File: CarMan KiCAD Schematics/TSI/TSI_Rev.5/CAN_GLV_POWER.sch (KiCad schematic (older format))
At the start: 35 parts, among them Q11 TN2130K1-G, U14 MountingHole, U15 MountingHole, U17 ChassisGND, U2 SFS2-DC24V, U24 TLP293, U28 MountingHole, U33 SFS2-DC24V, U41 PDQ10-Q24-D5-D, U42 LT1763CS8-3.3PBF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

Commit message: TSI Footprints - Res, Caps, Inductor all 0805s - Mounting Holes
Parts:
- removed U17: ChassisGND, symbol Mechanical:MountingHole
- added U17: Chassis Ground, MountingHole:MountingHole_3.5mm_Pad, symbol Mechanical:MountingHole_Pad
- C13, C18, C56, C57, C58, C59, C60, C61: footprint (none) -> Capacitor_SMD:C_0805_2012Metric_Pad1.15x1.40mm_HandSolder
- R45, R52, R55, R57, R71, R72, R79, R92: footprint (none) -> Resistor_SMD:R_0805_2012Metric_Pad1.15x1.40mm_HandSolder
- U14, U15, U28: footprint (none) -> MountingHole:MountingHole_3.5mm_Pad
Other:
- moved on the sheet: U14, U15, U28
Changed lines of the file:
@@
 L Mechanical:MountingHole U14
 U 1 1 5FB208C3
-P 900 800
-F 0 "U14" H 800 950 50  0000 L CNN
-F 1 "MountingHole" H 650 650 50  0000 L CNN
-F 2 "" H 900 800 50  0001 C CNN
-F 3 "~" H 900 800 50  0001 C CNN
-	1    900  800
+P 800 800
+F 0 "U14" H 700 950 50  0000 L CNN
+F 1 "MountingHole" H 550 650 50  0000 L CNN
+F 2 "MountingHole:MountingHole_3.5mm_Pad" H 800 800 50  0001 C CNN
+F 3 "~" H 800 800 50  0001 C CNN
+	1    800  800
 	1    0    0    -1
 $EndComp
@@
 L Mechanical:MountingHole U15
 U 1 1 5FB22D5E
-P 1550 800
-F 0 "U15" H 1450 950 50  0000 L CNN
-F 1 "MountingHole" H 1300 650 50  0000 L CNN
-F 2 "" H 1550 800 50  0001 C CNN
-F 3 "~" H 1550 800 50  0001 C CNN
-	1    1550 800
+P 1450 800
+F 0 "U15" H 1350 950 50  0000 L CNN
+F 1 "MountingHole" H 1200 650 50  0000 L CNN
+F 2 "MountingHole:MountingHole_3.5mm_Pad" H 1450 800 50  0001 C CNN
+F 3 "~" H 1450 800 50  0001 C CNN
+	1    1450 800
 	1    0    0    -1
 $EndComp
@@
 L Mechanical:MountingHole U28
 U 1 1 5FB236B2
-P 2200 800
-F 0 "U28" H 2100 950 50  0000 L CNN
-F 1 "MountingHole" H 1950 650 50  0000 L CNN
-F 2 "" H 2200 800 50  0001 C CNN
-F 3 "~" H 2200 800 50  0001 C CNN
-	1    2200 800
-	1    0    0    -1
-$EndComp
-$Comp
-L Mechanical:MountingHole U17
-U 1 1 5FB23CBE
-P 900 1250
-F 0 "U17" H 700 1350 50  0000 L CNN
-F 1 "ChassisGND" H 650 1100 50  0000 L CNN
-F 2 "" H 900 1250 50  0001 C CNN
-F 3 "~" H 900 1250 50  0001 C CNN
-	1    900  1250
+P 800 1300
+F 0 "U28" H 700 1450 50  0000 L CNN
+F 1 "MountingHole" H 550 1150 50  0000 L CNN
+F 2 "MountingHole:MountingHole_3.5mm_Pad" H 800 1300 50  0001 C CNN
+F 3 "~" H 800 1300 50  0001 C CNN
+	1    800  1300
 	1    0    0    -1
 $EndComp
@@
 F 0 "C57" H 1900 4900 50  0000 L CNN
 F 1 "10u" H 1850 4700 50  0000 L CNN
-F 2 "" H 1850 4800 50  0001 C CNN
+F 2 "Capacitor_SMD:C_0805_2012Metric_Pad1.15x1.40mm_HandSolder" H 1850 4800 50  0001 C CNN
 F 3 "~" H 1850 4800 50  0001 C CNN
 	1    1850 4800
@@
 F 0 "C56" H 1350 4900 50  0000 L CNN
 F 1 "10u" H 1350 4700 50  0000 L CNN
-F 2 "" H 1350 4800 50  0001 C CNN
+F 2 "Capacitor_SMD:C_0805_2012Metric_Pad1.15x1.40mm_HandSolder" H 1350 4800 50  0001 C CNN
 F 3 "~" H 1350 4800 50  0001 C CNN
 	1    1350 4800
@@
 F 0 "C58" H 4700 5300 50  0000 L CNN
 F 1 "0.1u" H 4700 5100 50  0000 L CNN
-F 2 "" H 4700 5200 50  0001 C CNN
+F 2 "Capacitor_SMD:C_0805_2012Metric_Pad1.15x1.40mm_HandSolder" H 4700 5200 50  0001 C CNN
 F 3 "~" H 4700 5200 50  0001 C CNN
 	1    4700 5200
@@
 F 0 "C59" H 5400 5550 50  0000 L CNN
 F 1 "1u" H 5400 5350 50  0000 L CNN
-F 2 "" H 5350 5450 50  0001 C CNN
+F 2 "Capacitor_SMD:C_0805_2012Metric_Pad1.15x1.40mm_HandSolder" H 5350 5450 50  0001 C CNN
 F 3 "~" H 5350 5450 50  0001 C CNN
 	1    5350 5450
@@
 F 0 "C60" H 5900 5350 50  0000 L CNN
 F 1 "1u" H 5900 5150 50  0000 L CNN
-F 2 "" H 6100 5250 50  0001 C CNN
+F 2 "Capacitor_SMD:C_0805_2012Metric_Pad1.15x1.40mm_HandSolder" H 6100 5250 50  0001 C CNN
 F 3 "~" H 6100 5250 50  0001 C CNN
 	1    6100 5250
@@
 Text Label 15050 1050 2    50   ~ 0
 CANRX
-Wire Wire Line
-	900  1250 1400 1250
-Text Label 1400 1250 0    50   ~ 0
+Text Label 2050 1300 2    50   ~ 0
 ChassisGND
 Text Notes 7750 4000 2    89   ~ 0
@@
 F 0 "C61" H 8150 5500 50  0000 L CNN
 F 1 "10u" H 8150 5300 50  0000 L CNN
-F 2 "" H 8100 5400 50  0001 C CNN
+F 2 "Capacitor_SMD:C_0805_2012Metric_Pad1.15x1.40mm_HandSolder" H 8100 5400 50  0001 C CNN
 F 3 "~" H 8100 5400 50  0001 C CNN
 	1    8100 5400
@@
 F 0 "R92" V 11000 3600 50  0000 C CNN
 F 1 "120" V 11100 3600 50  0000 C CNN
-F 2 "" V 11030 3600 50  0001 C CNN
+F 2 "Resistor_SMD:R_0805_2012Metric_Pad1.15x1.40mm_HandSolder" V 11030 3600 50  0001 C CNN
 F 3 "~" H 11100 3600 50  0001 C CNN
 	1    11100 3600
@@
 F 0 "R71" V 3900 1050 50  0000 C CNN
 F 1 "2.1K" V 4000 1050 50  0000 C CNN
-F 2 "" V 3930 1050 50  0001 C CNN
+F 2 "Resistor_SMD:R_0805_2012Metric_Pad1.15x1.40mm_HandSolder" V 3930 1050 50  0001 C CNN
 F 3 "~" H 4000 1050 50  0001 C CNN
 	1    4000 1050
@@
 F 0 "R79" H 10970 6196 50  0000 L CNN
 F 1 "10K" V 10900 6100 50  0000 L CNN
-F 2 "" V 10830 6150 50  0001 C CNN
+F 2 "Resistor_SMD:R_0805_2012Metric_Pad1.15x1.40mm_HandSolder" V 10830 6150 50  0001 C CNN
 F 3 "~" H 10900 6150 50  0001 C CNN
 	1    10900 6150
@@
 F 0 "R72" V 10650 5900 50  0000 C CNN
 F 1 "1K" V 10750 5900 50  0000 C CNN
-F 2 "" V 10680 5900 50  0001 C CNN
+F 2 "Resistor_SMD:R_0805_2012Metric_Pad1.15x1.40mm_HandSolder" V 10680 5900 50  0001 C CNN
 F 3 "~" H 10750 5900 50  0001 C CNN
 	1    10750 5900
@@
 F 0 "R45" V 9300 1300 50  0000 C CNN
 F 1 "2.4K" V 9400 1300 50  0000 C CNN
-F 2 "" V 9330 1300 50  0001 C CNN
+F 2 "Resistor_SMD:R_0805_2012Metric_Pad1.15x1.40mm_HandSolder" V 9330 1300 50  0001 C CNN
 F 3 "~" H 9400 1300 50  0001 C CNN
 	1    9400 1300
@@
 F 0 "R55" V 10450 1100 50  0000 C CNN
 F 1 "2.4K" V 10550 1100 50  0000 C CNN
-F 2 "" V 10480 1100 50  0001 C CNN
+F 2 "Resistor_SMD:R_0805_2012Metric_Pad1.15x1.40mm_HandSolder" V 10480 1100 50  0001 C CNN
 F 3 "~" H 10550 1100 50  0001 C CNN
 	1    10550 1100
@@
 F 0 "R52" H 12320 3346 50  0000 L CNN
 F 1 "1K" H 12350 3250 50  0000 L CNN
-F 2 "" V 12180 3300 50  0001 C CNN
+F 2 "Resistor_SMD:R_0805_2012Metric_Pad1.15x1.40mm_HandSolder" V 12180 3300 50  0001 C CNN
 F 3 "~" H 12250 3300 50  0001 C CNN
 	1    12250 3300
@@
 F 0 "R57" H 5270 1496 50  0000 L CNN
 F 1 "40K" H 5270 1405 50  0000 L CNN
-F 2 "" V 5130 1450 50  0001 C CNN
+F 2 "Resistor_SMD:R_0805_2012Metric_Pad1.15x1.40mm_HandSolder" V 5130 1450 50  0001 C CNN
 F 3 "~" H 5200 1450 50  0001 C CNN
 	1    5200 1450
@@
 F 0 "C18" H 6765 2446 50  0000 L CNN
 F 1 "10u" H 6765 2355 50  0000 L CNN
-F 2 "" H 6688 2250 50  0001 C CNN
+F 2 "Capacitor_SMD:C_0805_2012Metric_Pad1.15x1.40mm_HandSolder" H 6688 2250 50  0001 C CNN
 F 3 "~" H 6650 2400 50  0001 C CNN
 	1    6650 2400
@@
 F 0 "C13" H 4165 2446 50  0000 L CNN
 F 1 "100u" H 4165 2355 50  0000 L CNN
-F 2 "" H 4088 2250 50  0001 C CNN
+F 2 "Capacitor_SMD:C_0805_2012Metric_Pad1.15x1.40mm_HandSolder" H 4088 2250 50  0001 C CNN
 F 3 "~" H 4050 2400 50  0001 C CNN
 	1    4050 2400
@@
 Text Notes 3650 3000 0    55   ~ 0
 Control Signal used as a \npsuedo relay
+$Comp
+L Mechanical:MountingHole_Pad U17
+U 1 1 60035C0C
+P 1500 1300
+F 0 "U17" V 1650 1350 50  0000 C CNN
+F 1 "Chassis Ground" V 1350 1300 50  0000 C CNN
+F 2 "MountingHole:MountingHole_3.5mm_Pad" H 1500 1300 50  0001 C CNN
+F 3 "~" H 1500 1300 50  0001 C CNN
+	1    1500 1300
+	0    -1   -1   0
+$EndComp
+Wire Wire Line
+	1600 1300 2050 1300
 $EndSCHEMATC

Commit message: TSI Footprinting (~80%)  - Added Molex  - Added Current Sensor
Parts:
- 3.3V_TP1, 5V_TP1: footprint (none) -> TestPoint:TestPoint_Pad_D3.0mm
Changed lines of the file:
@@
 F 0 "5V_TP1" H 5008 4918 50  0000 L CNN
 F 1 "5V_TP" H 5008 4827 50  0000 L CNN
-F 2 "" H 5150 4800 50  0001 C CNN
+F 2 "TestPoint:TestPoint_Pad_D3.0mm" H 5150 4800 50  0001 C CNN
 F 3 "~" H 5150 4800 50  0001 C CNN
 	1    4950 4800
@@
 F 0 "3.3V_TP1" H 8150 4900 50  0001 L TNN
 F 1 "3.3V_TP" H 8150 4850 50  0000 L CNN
-F 2 "" H 8500 4650 50  0001 C CNN
+F 2 "TestPoint:TestPoint_Pad_D3.0mm" H 8500 4650 50  0001 C CNN
 F 3 "~" H 8500 4650 50  0001 C CNN
 	1    8300 4650

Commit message: TSI Footprinting (~90%)
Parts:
- D5, D9: footprint Diode_THT:D_DO-41_SOD81_P10.16mm_Horizontal -> Diode_THT:D_DO-41_SOD81_P7.62mm_Horizontal
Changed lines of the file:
@@
 F 0 "D9" H 3150 7500 50  0000 L CNN
 F 1 "1N4001" H 3050 7700 50  0000 L CNN
-F 2 "Diode_THT:D_DO-41_SOD81_P10.16mm_Horizontal" H 3200 7425 50  0001 C CNN
+F 2 "Diode_THT:D_DO-41_SOD81_P7.62mm_Horizontal" H 3200 7425 50  0001 C CNN
 F 3 "http://www.vishay.com/docs/88503/1n4001.pdf" H 3200 7600 50  0001 C CNN
 	1    3200 7600
@@
 F 0 "D5" H 8150 7450 50  0000 L CNN
 F 1 "1N4001" H 8050 7650 50  0000 L CNN
-F 2 "Diode_THT:D_DO-41_SOD81_P10.16mm_Horizontal" H 8200 7375 50  0001 C CNN
+F 2 "Diode_THT:D_DO-41_SOD81_P7.62mm_Horizontal" H 8200 7375 50  0001 C CNN
 F 3 "http://www.vishay.com/docs/88503/1n4001.pdf" H 8200 7550 50  0001 C CNN
 	1    8200 7550

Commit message: Bug Fixins
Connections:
- net labels removed: ChassisGND
- wire segments 179 -> 177
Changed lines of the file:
@@
 Wire Wire Line
 	4700 4950 4700 4800
-Wire Wire Line
-	3650 4800 4550 4800
-$Comp
-L power:PWR_FLAG #FLG03
-U 1 1 5FB2DC71
-P 4550 4800
-F 0 "#FLG03" H 4550 4875 50  0001 C CNN
-F 1 "PWR_FLAG" H 4450 4750 50  0000 C CNN
-F 2 "" H 4550 4800 50  0001 C CNN
-F 3 "~" H 4550 4800 50  0001 C CNN
-	1    4550 4800
-	1    0    0    -1
-$EndComp
-Connection ~ 4550 4800
-Wire Wire Line
-	4550 4800 4700 4800
 $Comp
 L pspice:CAP C59
@@
 CANRX
 Text Label 2050 1300 2    50   ~ 0
-ChassisGND
+Chassis_GND
 Text Notes 7750 4000 2    89   ~ 0
 3.3V REGULATOR
@@
 Wire Wire Line
 	3650 4700 4350 4700
-$Comp
-L power:PWR_FLAG #FLG0103
-U 1 1 60AD6C72
-P 4350 4700
-F 0 "#FLG0103" H 4350 4775 50  0001 C CNN
-F 1 "PWR_FLAG" H 4350 4873 50  0000 C CNN
-F 2 "" H 4350 4700 50  0001 C CNN
-F 3 "~" H 4350 4700 50  0001 C CNN
-	1    4350 4700
-	1    0    0    -1
-$EndComp
 Text Notes 10950 1900 2    89   ~ 0
 AIRs power on SL closed
@@
 Text Notes 3700 2050 0    49   ~ 0
 DC/DC Converter 24V to 12V 10A
-Wire Wire Line
-	6450 2250 6650 2250
-Connection ~ 6450 2250
-$Comp
-L power:PWR_FLAG #FLG02
-U 1 1 5FBAC9F1
-P 6450 2250
-F 0 "#FLG02" H 6450 2325 50  0001 C CNN
-F 1 "PWR_FLAG" H 6450 2423 50  0000 C CNN
-F 2 "" H 6450 2250 50  0001 C CNN
-F 3 "~" H 6450 2250 50  0001 C CNN
-	1    6450 2250
-	1    0    0    -1
-$EndComp
 Text Label 3250 2650 0    49   ~ 0
 GLV_RTN
@@
 Wire Wire Line
 	6650 2550 6650 2650
-Wire Wire Line
-	6250 2250 6450 2250
 Wire Wire Line
 	4950 2650 5050 2650
@@
 Wire Wire Line
 	1600 1300 2050 1300
+Wire Wire Line
+	6250 2250 6650 2250
+Wire Wire Line
+	3650 4800 4700 4800
 $EndSCHEMATC

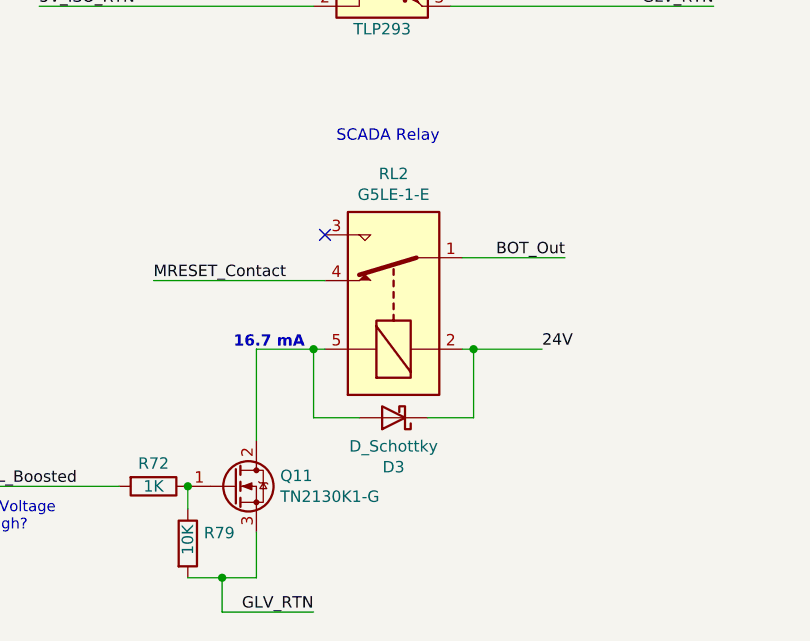
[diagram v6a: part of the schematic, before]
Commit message: TSI Footprinting (~95%) - Added Silk Screen Images from last years projects (not added to any libraries, just folder)
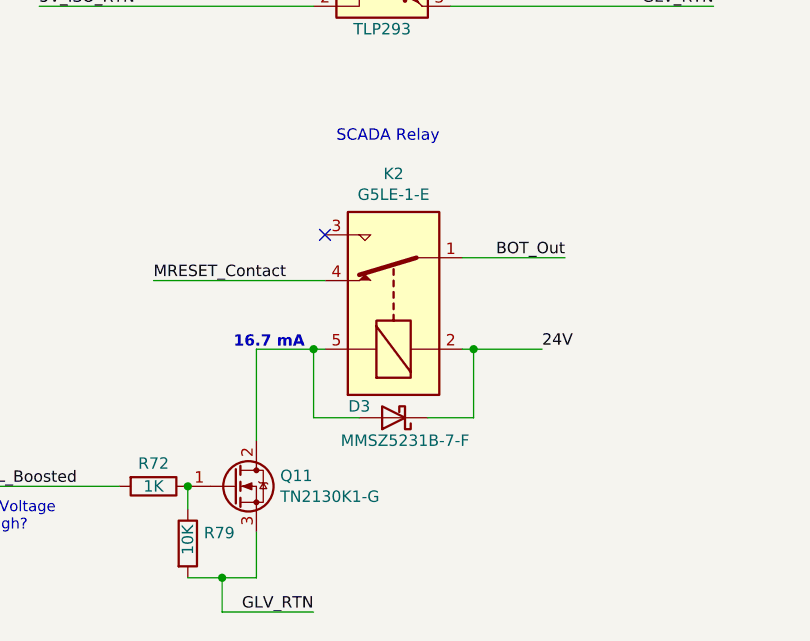
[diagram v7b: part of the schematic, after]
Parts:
- D3: value D_Schottky -> MMSZ5231B-7-F; footprint (none) -> Diode_SMD:D_SOD-123
- renumbered RL2 to K2
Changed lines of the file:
@@
 U 1 1 5FB8F043
 P 11800 5600
-F 0 "D3" H 11800 5816 50  0000 C CNN
-F 1 "D_Schottky" H 11800 5725 50  0000 C CNN
-F 2 "" H 11800 5600 50  0001 C CNN
+F 0 "D3" H 11950 5550 50  0000 C CNN
+F 1 "MMSZ5231B-7-F" H 11750 5700 50  0000 C CNN
+F 2 "Diode_SMD:D_SOD-123" H 11800 5600 50  0001 C CNN
 F 3 "~" H 11800 5600 50  0001 C CNN
 	1    11800 5600
@@
 P 11800 5100
 AR Path="/5FB466B1" Ref="RL?"  Part="1"
-AR Path="/5FE1DE7D/5FB466B1" Ref="RL2"  Part="1"
-F 0 "RL2" V 12367 5100 50  0000 C CNN
+AR Path="/5FE1DE7D/5FB466B1" Ref="K2"  Part="1"
+F 0 "K2" V 12367 5100 50  0000 C CNN
 F 1 "G5LE-1-E" V 12276 5100 50  0000 C CNN
 F 2 "" H 12050 5700 50  0001 C CNN

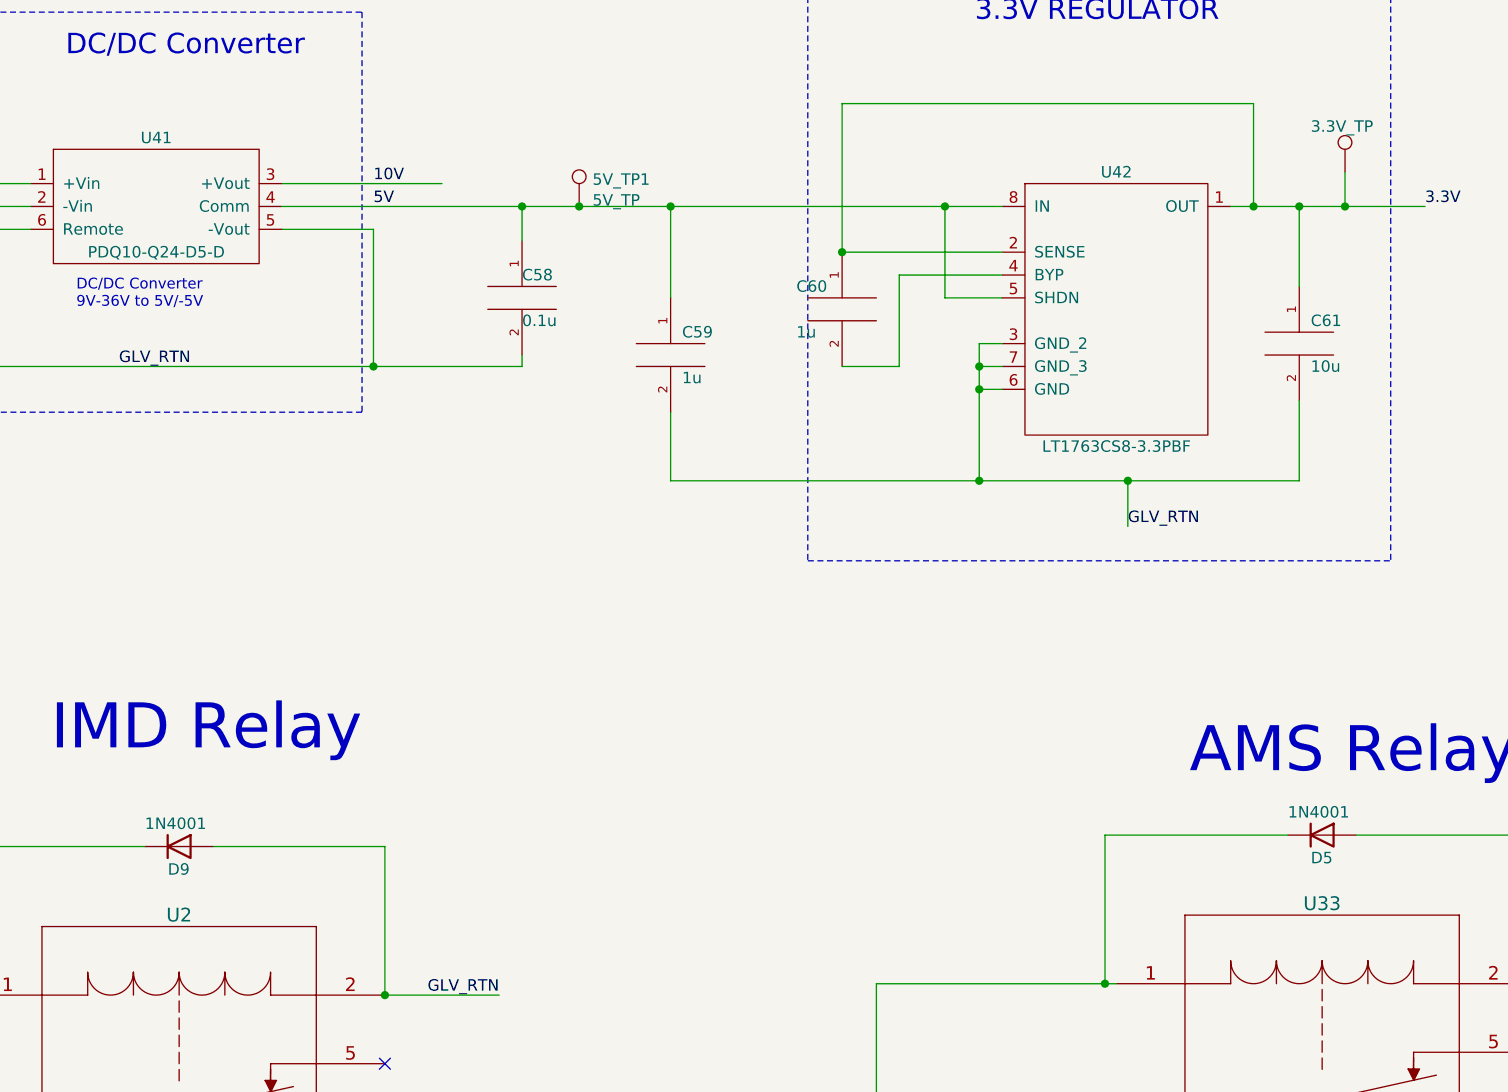
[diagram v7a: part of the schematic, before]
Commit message: TSI Footprinting (~98%) - Assigned U41 footprint to PS1 footprint. Not able to find PS1 footprint. Referenced last years design and took measurement on PCB. Measured as the same distances between points - Need footprints for K2, K3, K4 & J1
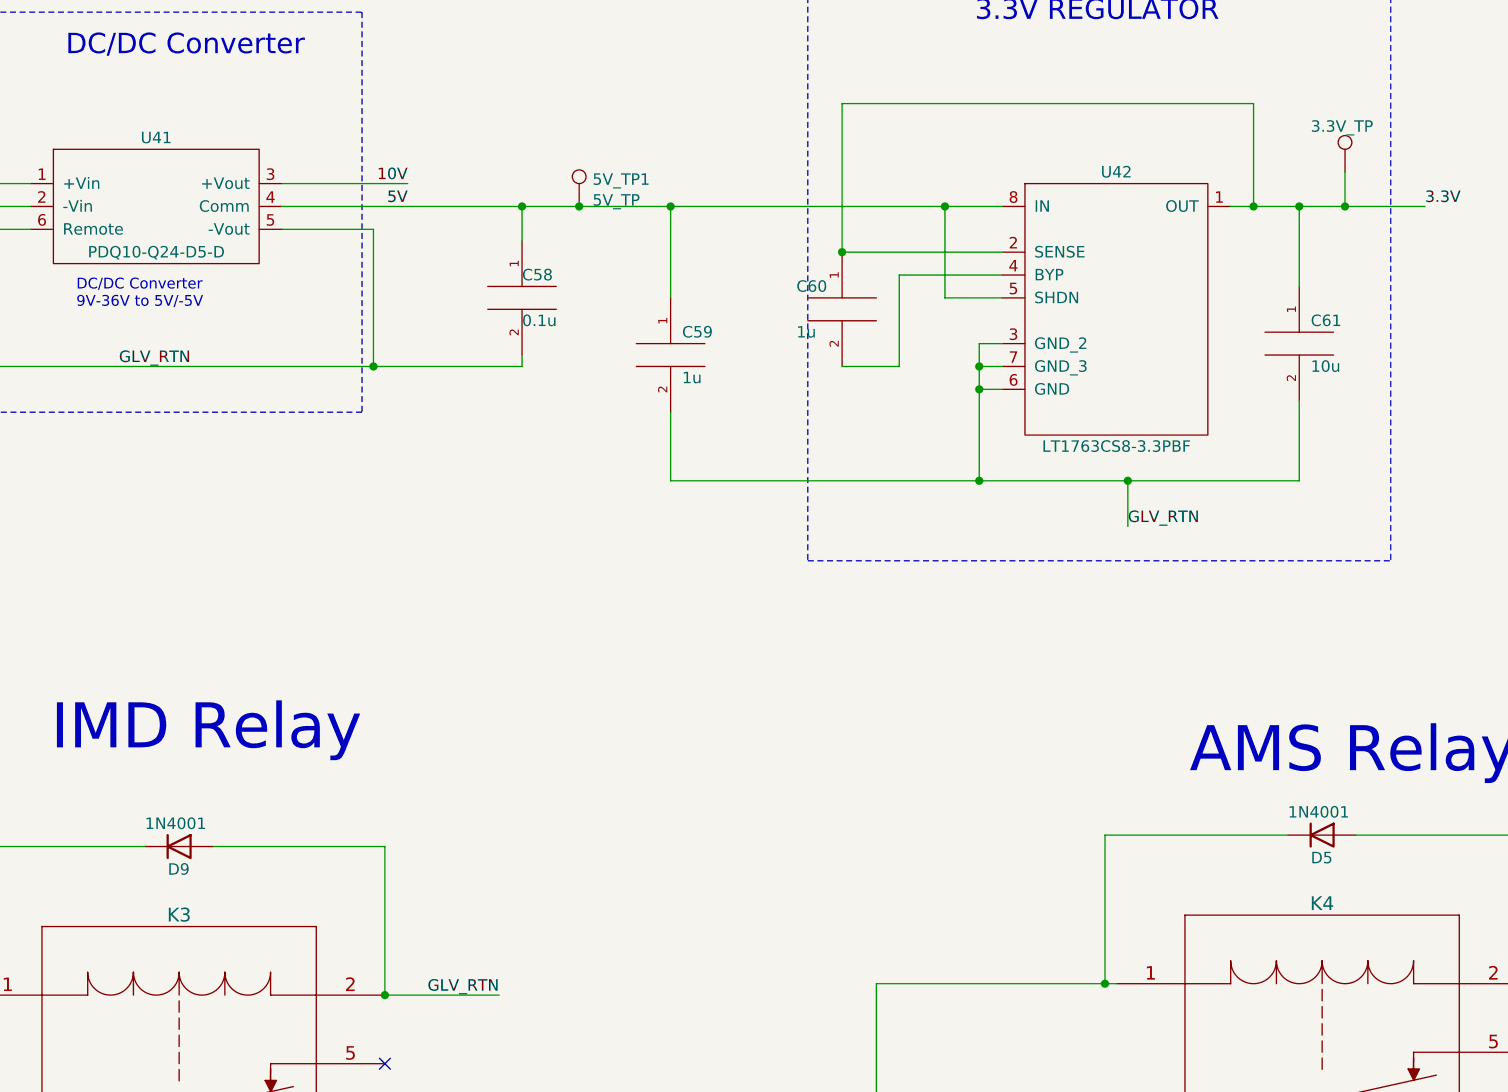
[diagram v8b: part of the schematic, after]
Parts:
- PS2: footprint CONV_EHHD010A0B41-HZ -> TSI_Rev_2021_Footprint_Lib:CONV_EHHD010A0B41-HZ
- renumbered U2 to K3, U33 to K4
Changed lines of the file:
@@
 $Descr A3 16535 11693
 encoding utf-8
-Sheet 5 6
+Sheet 4 6
 Title ""
 Date ""
@@
 Wire Wire Line
 	1150 5050 1000 5050
-Text Label 4050 4700 0    50   ~ 0
+Text Label 4200 4700 2    50   ~ 0
 10V
-Text Label 4050 4800 0    50   ~ 0
+Text Label 4200 4800 2    50   ~ 0
 5V
 $Comp
@@
 Text Label 7050 2250 2    49   ~ 0
 12V
-Wire Wire Line
-	3650 4700 4350 4700
 Text Notes 10950 1900 2    89   ~ 0
 AIRs power on SL closed
@@
 Connection ~ 4100 8250
 $Comp
-L CarMan_KiCAD_Library:SFS2-DC24V U2
+L CarMan_KiCAD_Library:SFS2-DC24V K3
 U 1 1 6014EB6D
 P 3200 9350
-F 0 "U2" H 3200 10800 60  0000 C CNN
+F 0 "K3" H 3200 10800 60  0000 C CNN
 F 1 "SFS2-DC24V" H 3200 8100 60  0000 C CNN
 F 2 "RELAY_SFS_PAN" H 4100 9690 60  0001 C CNN
@@
 SL1_Out
 $Comp
-L CarMan_KiCAD_Library:SFS2-DC24V U33
+L CarMan_KiCAD_Library:SFS2-DC24V K4
 U 1 1 5FC41168
 P 8200 9300
-F 0 "U33" H 8200 10750 60  0000 C CNN
+F 0 "K4" H 8200 10750 60  0000 C CNN
 F 1 "SFS2-DC24V" H 8200 8050 60  0000 C CNN
 F 2 "RELAY_SFS_PAN" H 9100 9640 60  0001 C CNN
@@
 F 0 "PS2" H 5650 3317 50  0000 C CNN
 F 1 "EHHD010A0B41-HZ" H 5650 3226 50  0000 C CNN
-F 2 "CONV_EHHD010A0B41-HZ" H 5650 2650 50  0001 L BNN
+F 2 "TSI_Rev_2021_Footprint_Lib:CONV_EHHD010A0B41-HZ" H 5650 2650 50  0001 L BNN
 F 3 "https://library.industrialsolutions.abb.com/publibrary/checkout/DS-EHHD010A0B?TNR=Data%20Sheets|DS-EHHD010A0B|PDF" H 5650 2650 50  0001 L BNN
 F 4 "Manufacturer Recommendations" H 5650 2650 50  0001 L BNN "STANDARD"
@@
 Wire Wire Line
 	3650 4800 4700 4800
+Wire Wire Line
+	3650 4700 4200 4700
 $EndSCHEMATC
